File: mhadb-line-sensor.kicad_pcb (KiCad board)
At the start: 2 copper layers, 0 parts

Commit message: pcb: import footprints from schema
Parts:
- added C1: 10u, Capacitor_SMD:C_0805_2012Metric, F.Cu at (89.3, 178.2)
- added C10: 0u1, Capacitor_SMD:C_0402_1005Metric, F.Cu at (67.8, 173.0)
- added C11: 0u1, Capacitor_SMD:C_0402_1005Metric, F.Cu at (67.8, 175.0)
- added C12: 1u, Capacitor_SMD:C_0402_1005Metric, F.Cu at (67.8, 177.0)
- added C13: 1u, Capacitor_SMD:C_0402_1005Metric, F.Cu at (70.6, 165.2)
- added C14: 10n, Capacitor_SMD:C_0402_1005Metric, F.Cu at (70.6, 167.1)
- added C15: 47u, Capacitor_SMD:C_1206_3216Metric, F.Cu at (66.1, 152.4)
- added C16: 47u, Capacitor_SMD:C_1206_3216Metric, F.Cu at (66.1, 155.8)
- added C17: 0u1, Capacitor_SMD:C_0402_1005Metric, F.Cu at (70.6, 169.1)
- added C18: 0u1, Capacitor_SMD:C_0402_1005Metric, F.Cu at (70.6, 171.1)
- added C19: 0u1, Capacitor_SMD:C_0402_1005Metric, F.Cu at (70.6, 173.0)
- added C2: 0u1, Capacitor_SMD:C_0402_1005Metric, F.Cu at (67.8, 165.2)
- added C20: 0u1, Capacitor_SMD:C_0402_1005Metric, F.Cu at (70.6, 175.0)
- added C21: 0u1, Capacitor_SMD:C_0402_1005Metric, F.Cu at (70.6, 177.0)
- added C22: 0u1, Capacitor_SMD:C_0402_1005Metric, F.Cu at (73.5, 165.2)
- added C23: 0u1, Capacitor_SMD:C_0402_1005Metric, F.Cu at (73.5, 167.1)
- added C24: 0u1, Capacitor_SMD:C_0402_1005Metric, F.Cu at (73.5, 169.1)
- added C25: 0u1, Capacitor_SMD:C_0402_1005Metric, F.Cu at (73.5, 171.1)
- added C26: 0u1, Capacitor_SMD:C_0402_1005Metric, F.Cu at (73.5, 173.0)
- added C3: 10u, Capacitor_SMD:C_0805_2012Metric, F.Cu at (89.3, 181.2)
- added C4: 10u, Capacitor_SMD:C_0805_2012Metric, F.Cu at (89.3, 184.2)
- added C5: 0u1, Capacitor_SMD:C_0402_1005Metric, F.Cu at (67.8, 167.1)
- added C6: 20p, Capacitor_SMD:C_0603_1608Metric, F.Cu at (76.9, 165.4)
- added C7: 20p, Capacitor_SMD:C_0603_1608Metric, F.Cu at (76.9, 167.9)
- added C8: 0u1, Capacitor_SMD:C_0402_1005Metric, F.Cu at (67.8, 169.1)
- added C9: 0u1, Capacitor_SMD:C_0402_1005Metric, F.Cu at (67.8, 171.1)
- added D1: GREEN, LED_SMD:LED_0805_2012Metric, F.Cu at (89.2, 165.7)
- added D10: H5VU10U, GLCS:Diode_DFN1006, F.Cu at (64.9, 179.1)
- added D11: YELLOW, LED_SMD:LED_0805_2012Metric, F.Cu at (89.2, 168.7)
- added D12: WS2812B, LED_SMD:LED_WS2812B_PLCC4_5.0x5.0mm_P3.2mm, F.Cu at (44.0, 139.7)
- added D13: WS2812B, LED_SMD:LED_WS2812B_PLCC4_5.0x5.0mm_P3.2mm, F.Cu at (44.0, 146.3)
- added D14: WS2812B, LED_SMD:LED_WS2812B_PLCC4_5.0x5.0mm_P3.2mm, F.Cu at (44.0, 152.9)
- added D15: WS2812B, LED_SMD:LED_WS2812B_PLCC4_5.0x5.0mm_P3.2mm, F.Cu at (44.0, 159.5)
- added D16: WS2812B, LED_SMD:LED_WS2812B_PLCC4_5.0x5.0mm_P3.2mm, F.Cu at (44.0, 166.1)
- added D17: WS2812B, LED_SMD:LED_WS2812B_PLCC4_5.0x5.0mm_P3.2mm, F.Cu at (52.2, 139.7)
- added D18: WS2812B, LED_SMD:LED_WS2812B_PLCC4_5.0x5.0mm_P3.2mm, F.Cu at (52.2, 146.3)
- added D19: WS2812B, LED_SMD:LED_WS2812B_PLCC4_5.0x5.0mm_P3.2mm, F.Cu at (52.2, 152.9)
- added D2: WHITE, LED_SMD:LED_0603_1608Metric, F.Cu at (89.0, 175.1)
- added D20: WS2812B, LED_SMD:LED_WS2812B_PLCC4_5.0x5.0mm_P3.2mm, F.Cu at (52.2, 159.5)
- added D21: WS2812B, LED_SMD:LED_WS2812B_PLCC4_5.0x5.0mm_P3.2mm, F.Cu at (52.2, 166.1)
- added D3: H5VU10U, GLCS:Diode_DFN1006, F.Cu at (64.9, 165.2)
- added D4: H5VU10U, GLCS:Diode_DFN1006, F.Cu at (64.9, 167.2)
- added D5: H5VU10U, GLCS:Diode_DFN1006, F.Cu at (64.9, 169.2)
- added D6: H5VU10U, GLCS:Diode_DFN1006, F.Cu at (64.9, 171.1)
- added D7: H5VU10U, GLCS:Diode_DFN1006, F.Cu at (64.9, 173.1)
- added D8: H5VU10U, GLCS:Diode_DFN1006, F.Cu at (64.9, 175.1)
- added D9: H5VU10U, GLCS:Diode_DFN1006, F.Cu at (64.9, 177.1)
- added FB1: 600Ω@100M, Inductor_SMD:L_0805_2012Metric, F.Cu at (88.2, 147.4)
- added FID1: Fiducial, Fiducial:Fiducial_1mm_Mask2mm, F.Cu at (53.1, 171.2)
- added FID2: Fiducial, Fiducial:Fiducial_1mm_Mask2mm, F.Cu at (53.1, 174.8)
- added FID3: Fiducial, Fiducial:Fiducial_1mm_Mask2mm, F.Cu at (53.1, 178.3)
- added H1: MountingHole_Pad, MountingHole:MountingHole_2.2mm_M2_Pad_Via, F.Cu at (59.2, 171.9)
- added H2: MountingHole_Pad, MountingHole:MountingHole_2.2mm_M2_Pad_Via, F.Cu at (59.2, 177.9)
- added H3: MountingHole, MountingHole:ToolingHole_1.152mm, F.Cu at (52.6, 182.0)
- added H4: MountingHole, MountingHole:ToolingHole_1.152mm, F.Cu at (52.6, 184.5)
- added H5: MountingHole, MountingHole:ToolingHole_1.152mm, F.Cu at (52.6, 186.9)
- added J1: TC2030, Connector:Tag-Connect_TC2030-IDC-NL_2x03_P1.27mm_Vertical, F.Cu at (70.3, 180.5)
- added J2: Conn_01x04_Pin, Connector_PinHeader_2.54mm:PinHeader_1x04_P2.54mm_Vertical, F.Cu at (82.5, 153.1)
- added J3: Conn_01x04, Connector_JST:JST_PH_S4B-PH-K_1x04_P2.00mm_Horizontal, F.Cu at (83.3, 138.7)
- added J4: Conn_01x04_Pin, Connector_PinHeader_2.54mm:PinHeader_1x04_P2.54mm_Vertical, F.Cu at (87.1, 153.1)
- added JP1: Jumper_2_Small_Bridged, Jumper:SolderJumper-2_P1.3mm_Open_RoundedPad1.0x1.5mm, F.Cu at (89.1, 172.0)
- added R1: 5k1, Resistor_SMD:R_0402_1005Metric, F.Cu at (49.9, 181.8)
- added R10: 2k, Resistor_SMD:R_0603_1608Metric, F.Cu at (80.9, 167.9)
- added R11: 2k, Resistor_SMD:R_0603_1608Metric, F.Cu at (80.9, 170.4)
- added R12: 100, Capacitor_SMD:C_1206_3216Metric, F.Cu at (66.1, 159.2)
- added R13: 100, Capacitor_SMD:C_1206_3216Metric, F.Cu at (66.1, 162.5)
- added R14: 100, Capacitor_SMD:C_1206_3216Metric, F.Cu at (71.7, 152.4)
- added R15: 100, Capacitor_SMD:C_1206_3216Metric, F.Cu at (71.7, 155.8)
- added R16: 100, Capacitor_SMD:C_1206_3216Metric, F.Cu at (71.7, 159.2)
- added R17: 100, Capacitor_SMD:C_1206_3216Metric, F.Cu at (71.7, 162.5)
- added R18: 100, Capacitor_SMD:C_1206_3216Metric, F.Cu at (77.4, 152.4)
- added R19: 100, Capacitor_SMD:C_1206_3216Metric, F.Cu at (77.4, 155.8)
- added R2: 5k1, Resistor_SMD:R_0402_1005Metric, F.Cu at (49.9, 183.8)
- added R20: 100, Capacitor_SMD:C_1206_3216Metric, F.Cu at (77.4, 159.2)
- added R21: 100, Capacitor_SMD:C_1206_3216Metric, F.Cu at (77.4, 162.5)
- added R22: 2k, Resistor_SMD:R_0603_1608Metric, F.Cu at (80.9, 173.0)
- added R23: 2k, Resistor_SMD:R_0603_1608Metric, F.Cu at (80.9, 175.5)
- added R24: 2k, Resistor_SMD:R_0603_1608Metric, F.Cu at (85.0, 165.4)
- added R25: 2k, Resistor_SMD:R_0603_1608Metric, F.Cu at (85.0, 167.9)
- added R26: 2k, Resistor_SMD:R_0603_1608Metric, F.Cu at (85.0, 170.4)
- added R3: 120, Resistor_SMD:R_1206_3216Metric, F.Cu at (83.1, 147.7)
- added R4: 10k, Resistor_SMD:R_0402_1005Metric, F.Cu at (49.9, 185.8)
- added R5: 560, Resistor_SMD:R_0603_1608Metric, F.Cu at (76.9, 170.4)
- added R6: 5k1, Resistor_SMD:R_0402_1005Metric, F.Cu at (49.9, 187.8)
- added R7: 2k, Resistor_SMD:R_0603_1608Metric, F.Cu at (76.9, 173.0)
- added R8: 2k, Resistor_SMD:R_0603_1608Metric, F.Cu at (76.9, 175.5)
- added R9: 2k, Resistor_SMD:R_0603_1608Metric, F.Cu at (80.9, 165.4)
- added SW1: SW_Push, Button_Switch_SMD:SW_SPST_TS-1088-xR020, F.Cu at (59.7, 153.1)
- added SW2: SW_Push, Button_Switch_SMD:SW_SPST_TS-1088-xR020, F.Cu at (59.7, 157.6)
- added SW3: SW_Push, Button_Switch_SMD:SW_SPST_TS-1088-xR020, F.Cu at (59.7, 162.2)
- added SW4: SW_Push, Button_Switch_SMD:SW_SPST_TS-1088-xR020, F.Cu at (59.7, 166.7)
- added TP1: TestPoint, TestPoint:TestPoint_Pad_D2.0mm, F.Cu at (77.0, 178.8)
- added TP2: TestPoint, TestPoint:TestPoint_Pad_D2.0mm, F.Cu at (77.0, 182.8)
- added TP3: TestPoint, TestPoint:TestPoint_Pad_D2.0mm, F.Cu at (77.0, 186.8)
- added TP4: TestPoint, TestPoint:TestPoint_Pad_D2.0mm, F.Cu at (81.0, 178.8)
- added TP5: TestPoint, TestPoint:TestPoint_Pad_D2.0mm, F.Cu at (81.0, 182.8)
- added TP6: TestPoint, TestPoint:TestPoint_Pad_D2.0mm, F.Cu at (81.0, 186.8)
- added TP7: TestPoint, TestPoint:TestPoint_Pad_D2.0mm, F.Cu at (85.0, 178.8)
- added TP8: TestPoint, TestPoint:TestPoint_Pad_D2.0mm, F.Cu at (85.0, 182.8)
- added TP9: TestPoint, TestPoint:TestPoint_Pad_D2.0mm, F.Cu at (85.0, 186.8)
- added U1: HT753-1, Package_TO_SOT_SMD:SOT-89-3, F.Cu at (59.6, 184.0)
- added U10: QRE1113GR, OptoDevice:OnSemi_CASE100CY, F.Cu at (63.5, 147.2)
- added U11: QRE1113GR, OptoDevice:OnSemi_CASE100CY, F.Cu at (68.3, 147.2)
- added U12: QRE1113GR, OptoDevice:OnSemi_CASE100CY, F.Cu at (73.1, 147.2)
- added U13: QRE1113GR, OptoDevice:OnSemi_CASE100CY, F.Cu at (78.0, 147.2)
- added U2: SN65HVD230, Package_SO:SOIC-8_3.9x4.9mm_P1.27mm, F.Cu at (44.2, 184.2)
- added U3: STM32F103C8Tx, Package_QFP:LQFP-48_7x7mm_P0.5mm, F.Cu at (45.6, 175.1)
- added U4: QRE1113GR, OptoDevice:OnSemi_CASE100CY, F.Cu at (58.7, 140.0)
- added U5: QRE1113GR, OptoDevice:OnSemi_CASE100CY, F.Cu at (63.5, 140.0)
- added U6: QRE1113GR, OptoDevice:OnSemi_CASE100CY, F.Cu at (68.3, 140.0)
- added U7: QRE1113GR, OptoDevice:OnSemi_CASE100CY, F.Cu at (73.1, 140.0)
- added U8: QRE1113GR, OptoDevice:OnSemi_CASE100CY, F.Cu at (78.0, 140.0)
- added U9: QRE1113GR, OptoDevice:OnSemi_CASE100CY, F.Cu at (58.7, 147.2)
- added Y1: 8M, Crystal:Crystal_SMD_5032-2Pin_5.0x3.2mm, F.Cu at (70.0, 185.6)

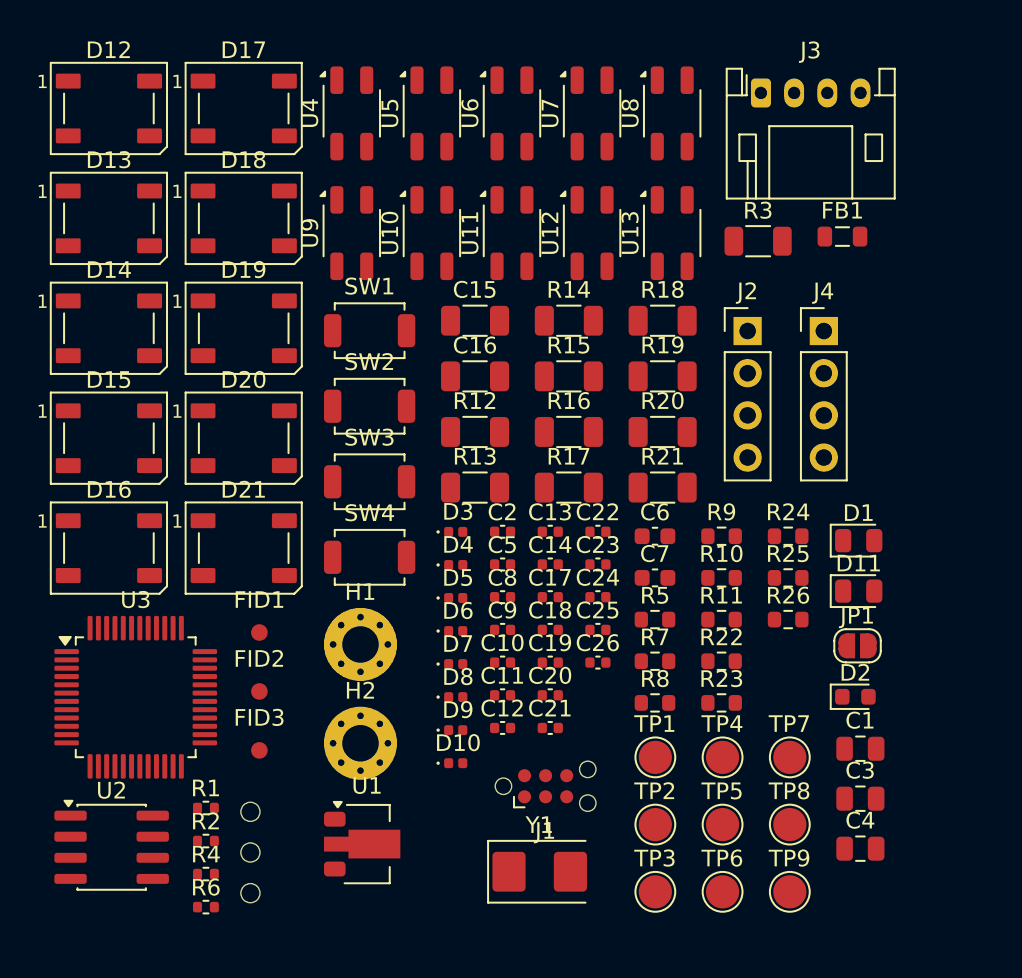
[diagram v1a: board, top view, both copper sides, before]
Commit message: schem/pcb: add EM stop btn
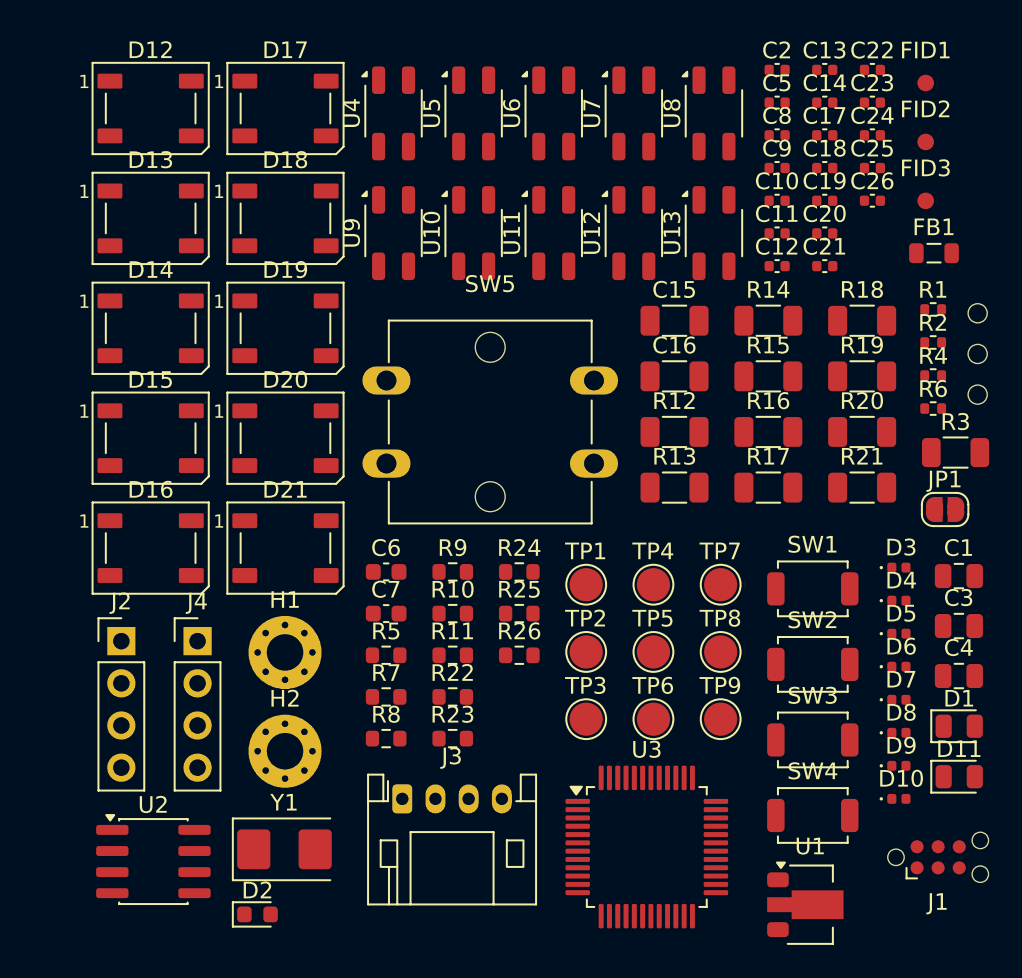
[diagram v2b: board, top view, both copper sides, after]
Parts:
- added SW5: SW_Push, Button_Switch_THT:SW_SPST_Omron_B3F-40xx, F.Cu at (60.8, 156.1)
- moved R1 53.1 mm to (93.7, 151.8)
- moved R2 53.1 mm to (93.7, 153.8)
- moved R4 53.1 mm to (93.7, 155.8)
- moved R6 53.1 mm to (93.7, 157.7)
- moved H3 53.1 mm to (96.4, 152.0)
- moved H4 53.1 mm to (96.4, 154.4)
- moved H5 53.1 mm to (96.4, 156.9)
- moved FID3 52.0 mm to (93.2, 145.2)
- moved FID1 52.0 mm to (93.2, 138.1)
- moved FID2 52.0 mm to (93.2, 141.7)
- moved J3 47.7 mm to (61.7, 181.2)
- moved J2 42.1 mm to (44.8, 171.8)
- moved J4 42.1 mm to (49.4, 171.8)
- moved D2 38.3 mm to (53.0, 188.2)
- moved C22 32.4 mm to (90.0, 137.3)
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
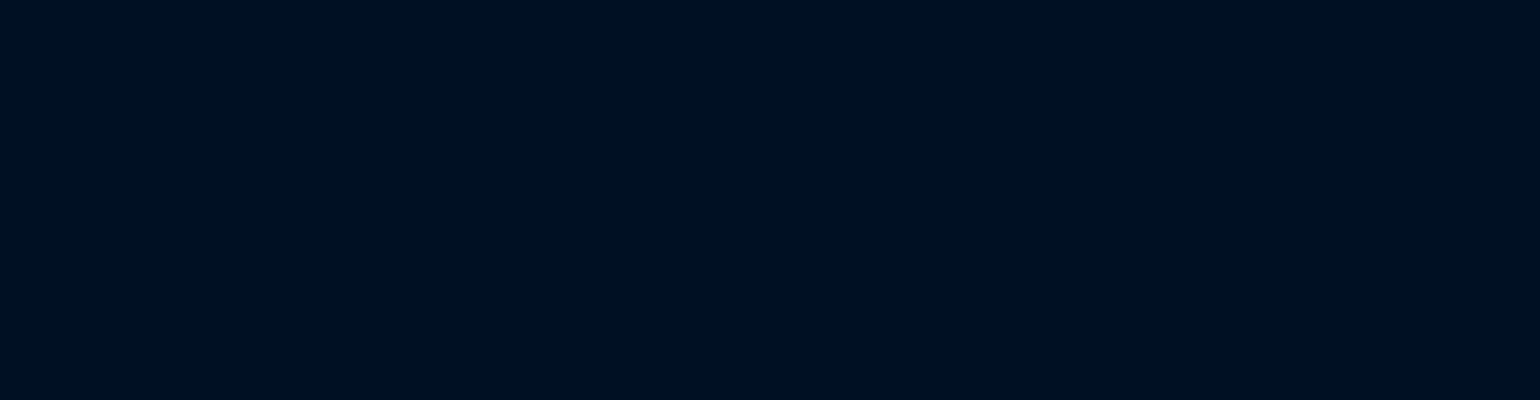
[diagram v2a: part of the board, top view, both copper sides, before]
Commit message: pcb: add board outline
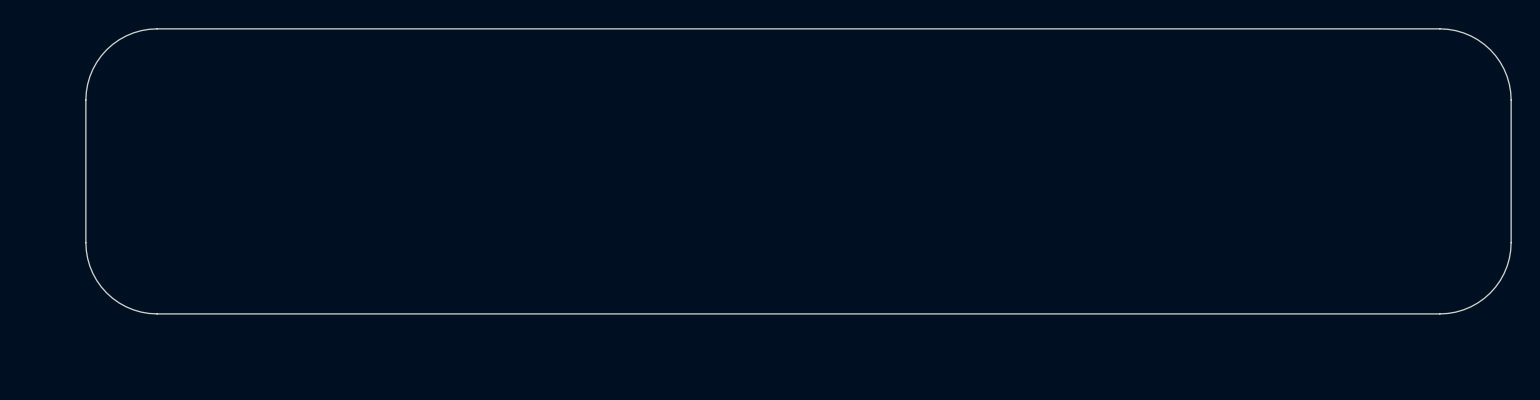
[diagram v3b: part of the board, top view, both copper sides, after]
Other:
- board outline added: 100 x 20 mm
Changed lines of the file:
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@@
 		)
+	)
+	(gr_line
+		(start 114 84)
+		(end 204 84)
+		(stroke
+			(width 0.05)
+			(type default)
+		)
+		(layer "Edge.Cuts")
+	)
+	(gr_arc
+		(start 109 89)
+		(mid 110.464466 85.464466)
+		(end 114 84)
+		(stroke
+			(width 0.05)
+			(type default)
+		)
+		(layer "Edge.Cuts")
+	)
+	(gr_line
+		(start 209 89)
+		(end 209 99)
+		(stroke
+			(width 0.05)
+			(type default)
+		)
+		(layer "Edge.Cuts")
+	)
+	(gr_arc
+		(start 209 99)
+		(mid 207.535534 102.535534)
+		(end 204 104)
+		(stroke
+			(width 0.05)
+			(type default)
+		)
+		(layer "Edge.Cuts")
+	)
+	(gr_arc
+		(start 204 84)
+		(mid 207.535534 85.464466)
+		(end 209 89)
+		(stroke
+			(width 0.05)
+			(type default)
+		)
+		(layer "Edge.Cuts")
+	)
+	(gr_line
+		(start 109 99)
+		(end 109 89)
+		(stroke
+			(width 0.05)
+			(type default)
+		)
+		(layer "Edge.Cuts")
+	)
+	(gr_arc
+		(start 114 104)
+		(mid 110.464466 102.535534)
+		(end 109 99)
+		(stroke
+			(width 0.05)
+			(type default)
+		)
+		(layer "Edge.Cuts")
+	)
+	(gr_line
+		(start 204 104)
+		(end 114 104)
+		(stroke
+			(width 0.05)
+			(type default)
+		)
+		(layer "Edge.Cuts")
 	)
 	(embedded_fonts no)

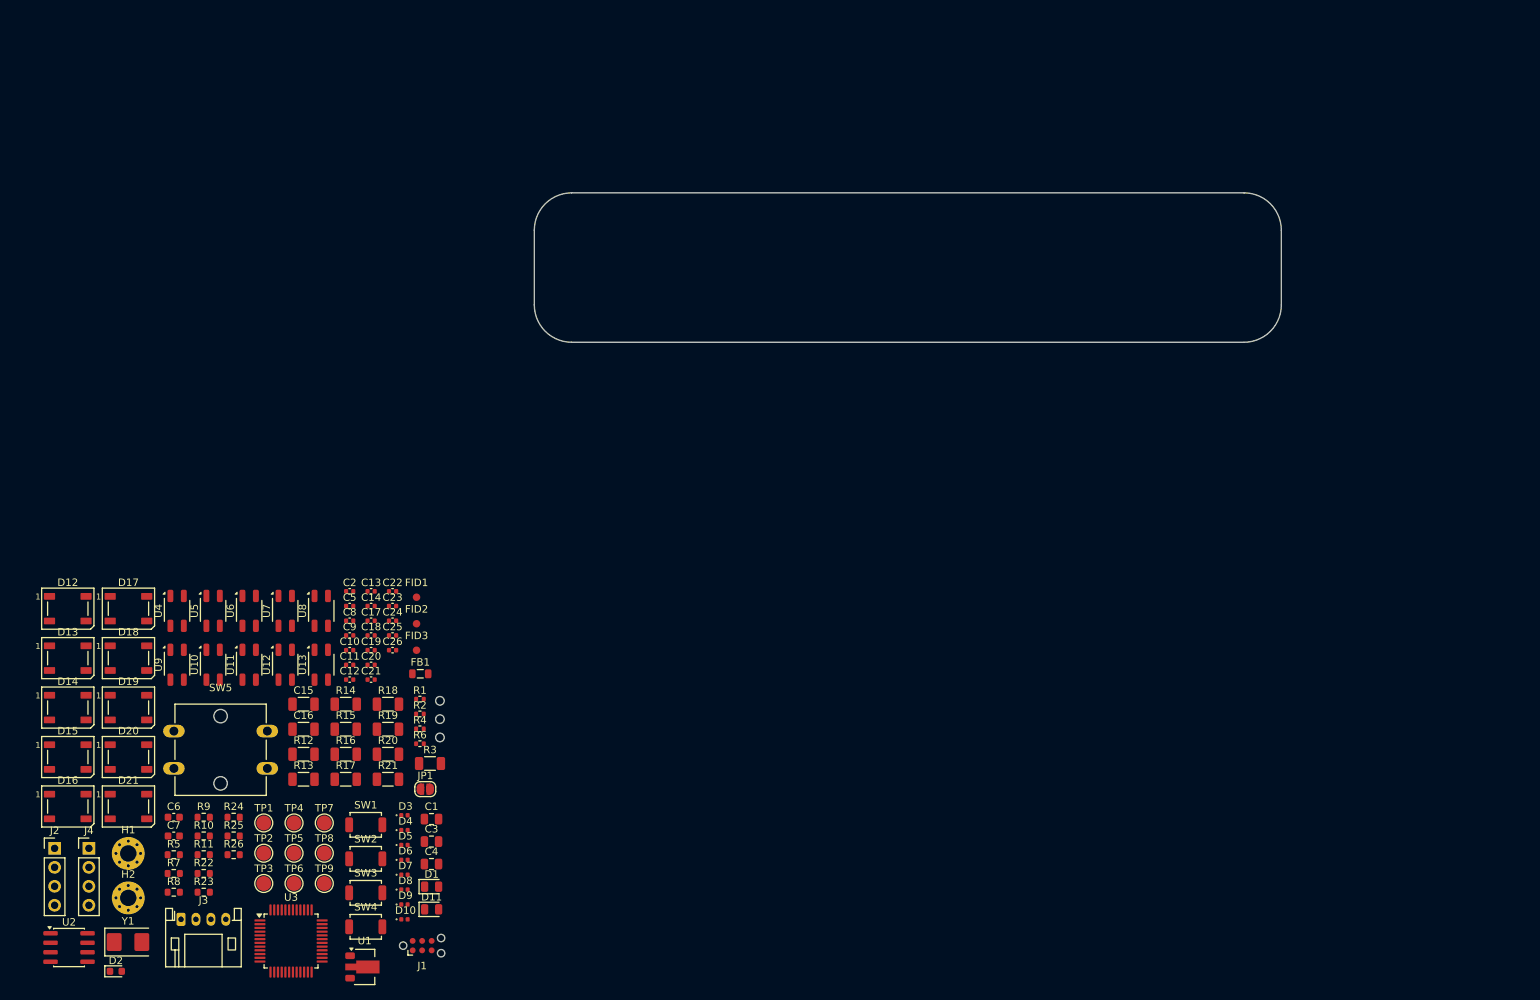
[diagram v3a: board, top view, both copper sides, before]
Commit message: pcb: initial sensor placement
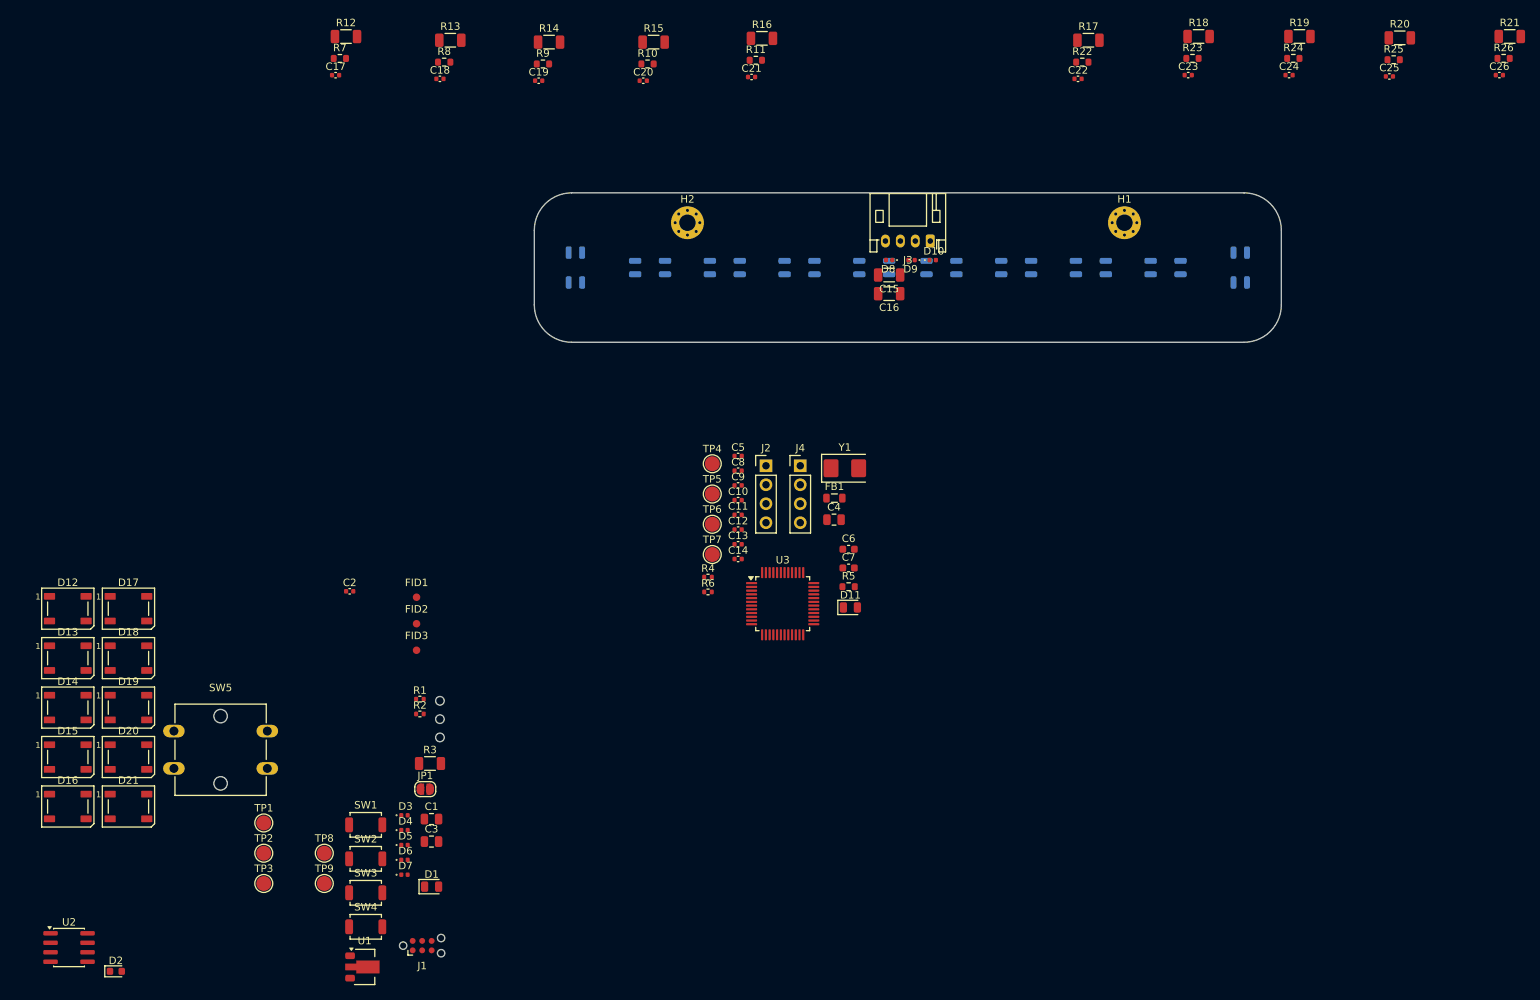
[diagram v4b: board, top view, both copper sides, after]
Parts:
- U10, U11, U12, U13, U4, U5, U6, U7, U8, U9: moved to B.Cu
- moved R26 200.7 mm to (238.8, 66.0)
- moved R25 186.8 mm to (224.0, 66.2)
- moved R21 180.1 mm to (239.6, 63.1)
- moved R24 174.5 mm to (210.6, 66.0)
- moved R23 173.1 mm to (197.1, 66.0)
- moved C26 167.0 mm to (238.2, 68.2)
- moved R20 166.0 mm to (224.9, 63.2)
- moved R22 160.1 mm to (182.4, 66.5)
- moved H1 157.8 mm to (188.0, 88.0)
- moved R19 153.3 mm to (211.4, 63.1)
- moved C25 153.0 mm to (223.5, 68.4)
- moved R18 140.6 mm to (197.9, 63.1)
- moved C24 140.5 mm to (210.0, 68.2)
- moved R17 140.3 mm to (183.2, 63.6)
- moved J3 135.3 mm to (162.0, 90.5), turned to 180 degrees
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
